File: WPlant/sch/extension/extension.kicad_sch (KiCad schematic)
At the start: 47 parts, among them J1 PROG/SWD, J2 HumSnc, J3 HumSnc, J4 HumSnc, J5 HumSnc, J6 Input, J7 Output, J8 LeakDetect, J9 Valves, Q1 FDS9926A, Q2 FDS9926A, U1 PY32F003F18P6TU, U2 74HC594, U3 74HC4052, U4 SP485EEN-L/TR, U6 AP2204R-5.0, U7 SP485EEN-L/TR

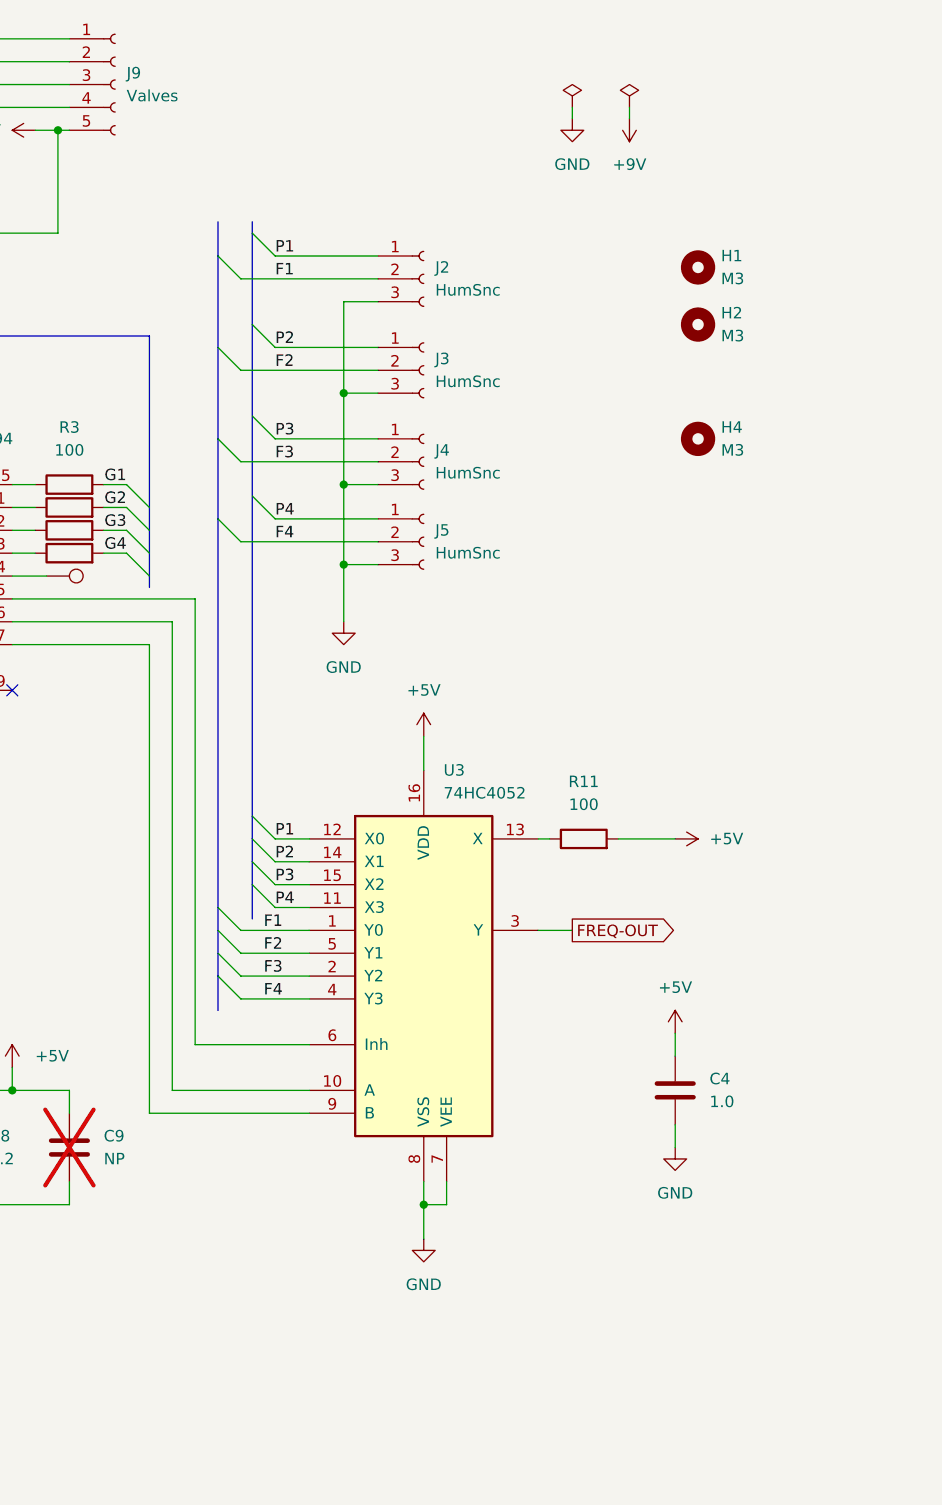
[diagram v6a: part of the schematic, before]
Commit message: Route of WP project done
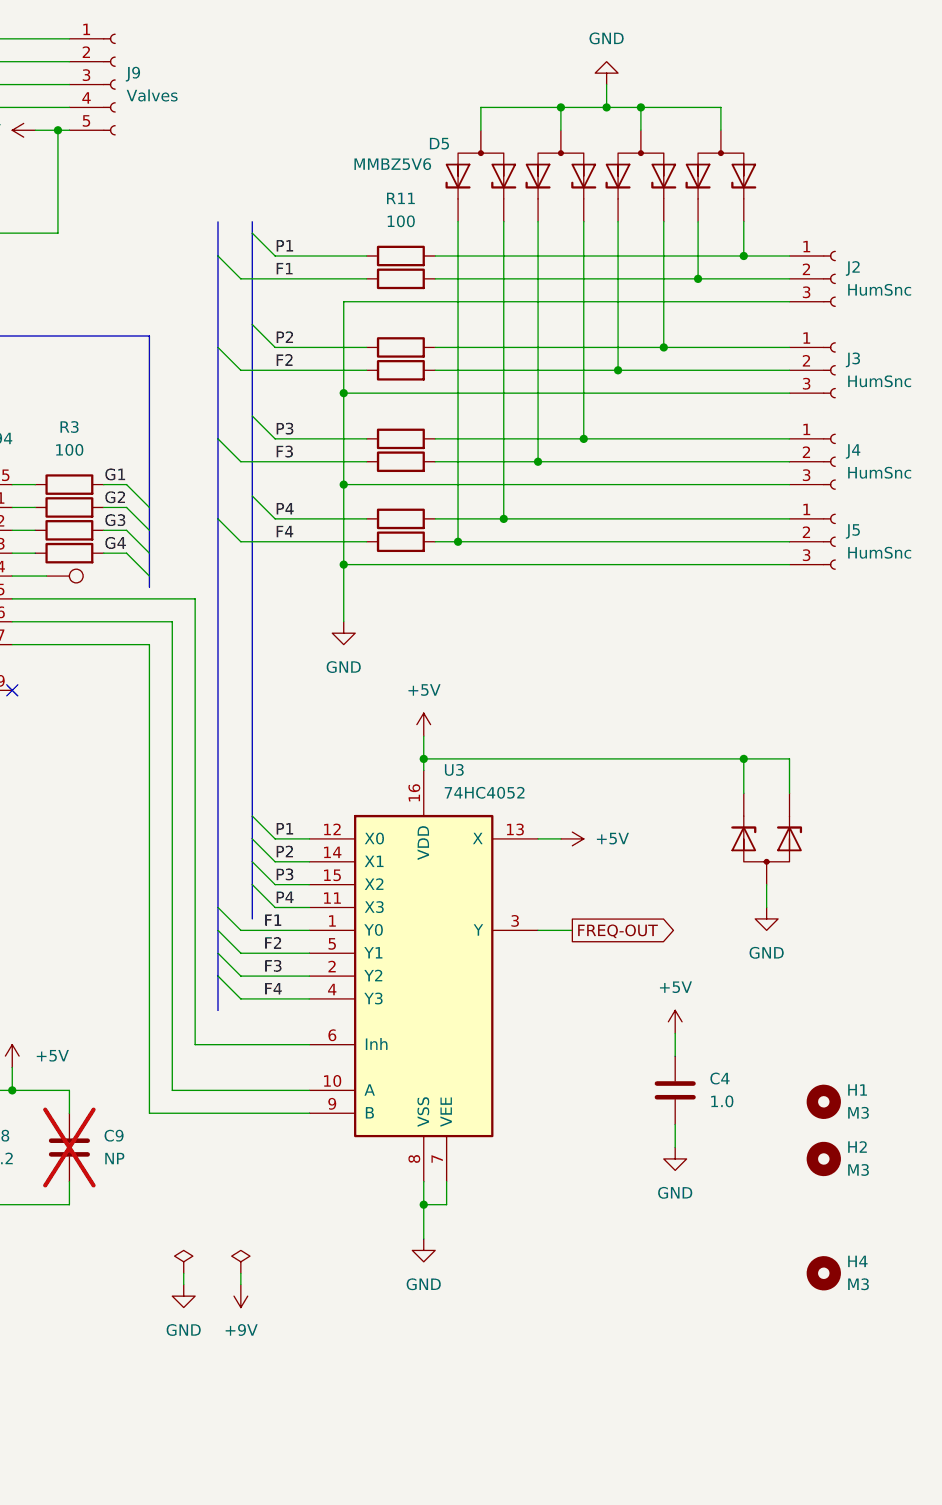
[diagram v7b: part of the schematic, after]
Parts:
- added D5, D6, D7, D8, D9: MMBZ5V6, Package_TO_SOT_SMD:SOT-23, symbol Diode:MMBZxx
- added R12, R13, R14, R15, R16, R17, R18: 100, Resistor_SMD:R_0603_1608Metric_Pad0.98x0.95mm_HandSolder, symbol Device:R
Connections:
- net +5V: now also U3.13 (X), D9.1 (K), D9.2 (K); no longer R11.2
- net F1: now also R12.1; no longer J2.2 (Pin_2)
- net F2: now also R14.1; no longer J3.2 (Pin_2)
- net F3: now also R16.1; no longer J4.2 (Pin_2)
- net F4: now also R18.1; no longer J5.2 (Pin_2)
- net GND: now also D5.3 (A), D6.3 (A), D7.3 (A), D8.3 (A), D9.3 (A)
- net P1: now also R11.1; no longer J2.1 (Pin_1)
- net P2: now also R13.1; no longer J3.1 (Pin_1)
- net P3: now also R15.1; no longer J4.1 (Pin_1)
- net P4: now also R17.1; no longer J5.1 (Pin_1)
- new net: D7.1 (K), J3.1 (Pin_1), R13.2
- new net: D7.2 (K), J3.2 (Pin_2), R14.2
- new net: D8.1 (K), J2.1 (Pin_1), R11.2
- new net: D8.2 (K), J2.2 (Pin_2), R12.2
- new net: D5.1 (K), J5.1 (Pin_1), R17.2
- new net: D5.2 (K), J5.2 (Pin_2), R18.2
- new net: D6.1 (K), J4.1 (Pin_1), R15.2
- new net: D6.2 (K), J4.2 (Pin_2), R16.2
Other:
- moved on the sheet: H1, H2, H4, J2, J3, J4, J5, R11

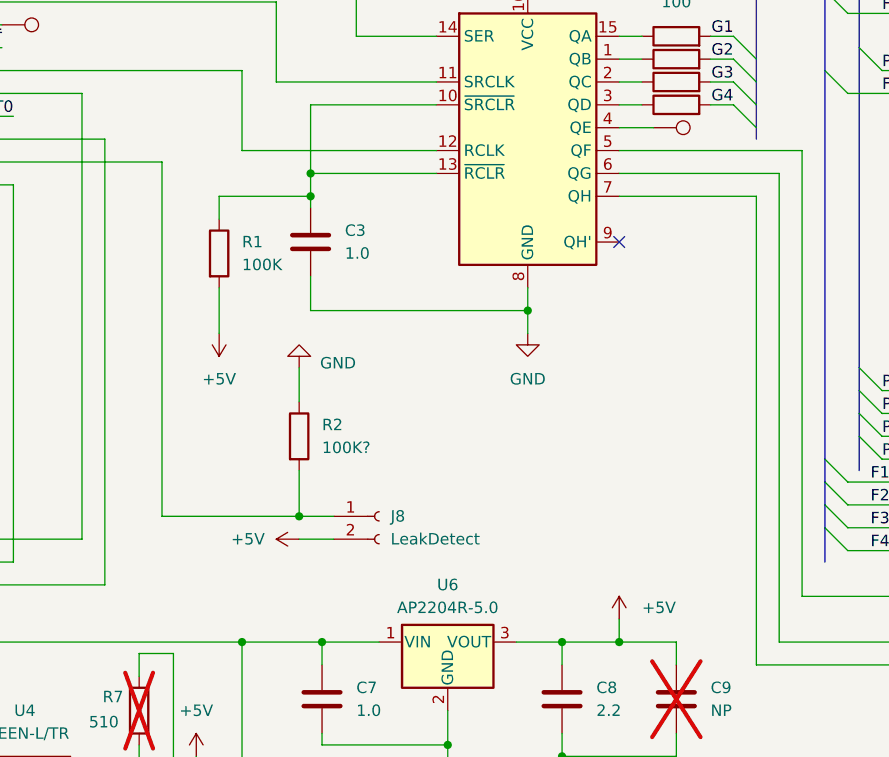
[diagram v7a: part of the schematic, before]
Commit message: Upate values in SCH of WP
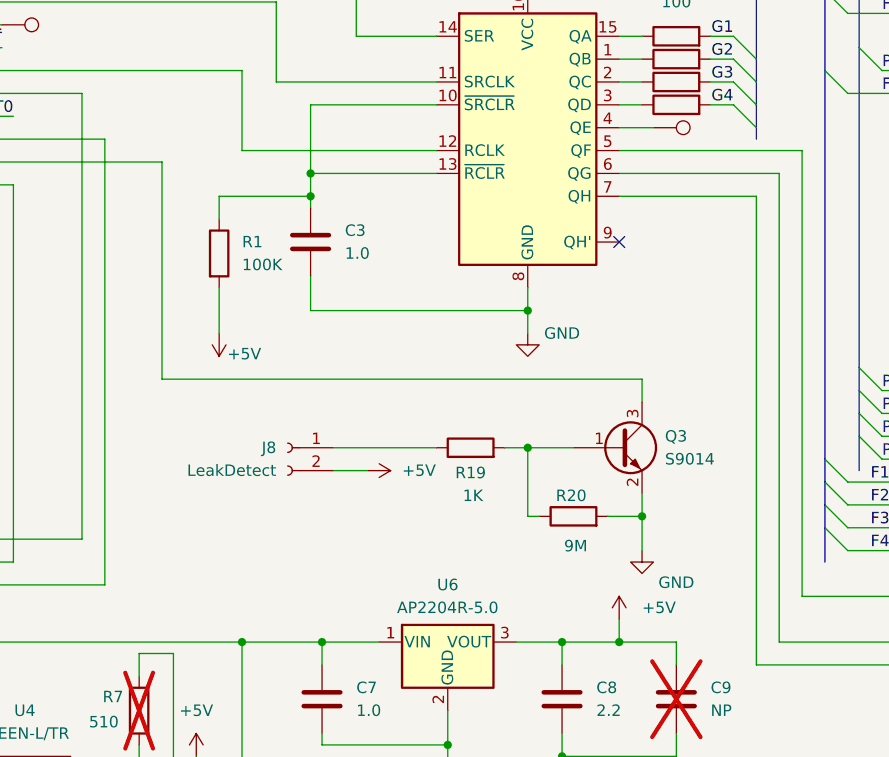
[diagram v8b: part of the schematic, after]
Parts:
- removed R2: 100K?, Resistor_SMD:R_0603_1608Metric_Pad0.98x0.95mm_HandSolder, symbol Device:R
- added Q3: S9014, Package_TO_SOT_SMD:SOT-23, symbol Device:Q_NPN_BEC
- added R19: 1K, Resistor_SMD:R_0603_1608Metric_Pad0.98x0.95mm_HandSolder, symbol Device:R
- added R20: 9M, Resistor_SMD:R_0603_1608Metric_Pad0.98x0.95mm_HandSolder, symbol Device:R
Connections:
- net GND: now also Q3.2 (E), R20.2
- net at J8.1 (Pin_1): now also R19.1; no longer U1.13 (PB6)
- new net: Q3.1 (B), R19.2, R20.1
- new net: Q3.3 (C), U1.13 (PB6)
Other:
- moved on the sheet: J8
